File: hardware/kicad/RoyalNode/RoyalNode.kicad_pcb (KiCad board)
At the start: 4 copper layers, 85 x 75 mm, 14 parts, among them J1 XT30PW-M C431092 RC, J2 XT30PW-M C431092 RC, J5 SMA edge envelope, Q1 Infineon PG-DSO-8-27 thermal 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, Q2 Infineon PG-DSO-8-27 thermal 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, Q3 Infineon PG-DSO-8-27 thermal 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, U1 BQ25798 RQM0029A RC, U2 LM66100 DCK0006A SC70-6 RC, U3 TPS61088 RHL0020A thermal via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, U4 LTC4365 TSOT-23-8 RC

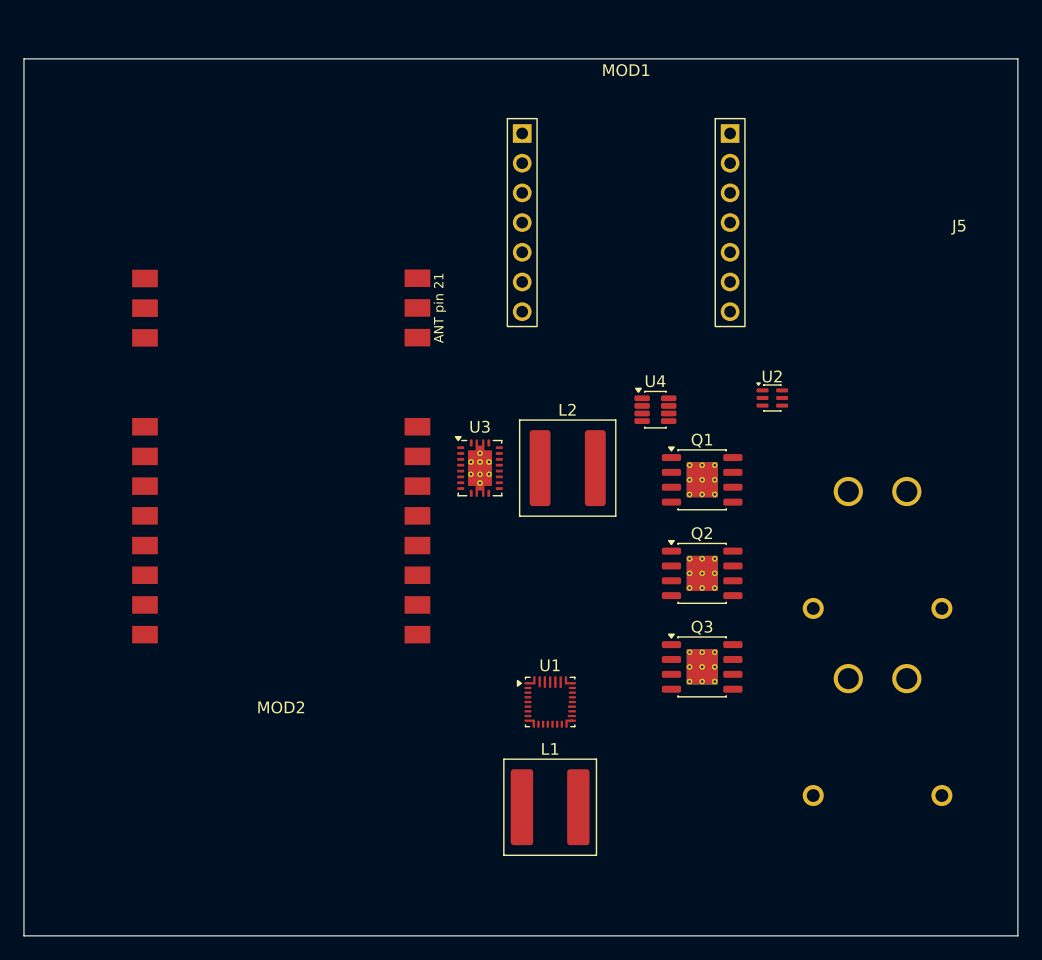
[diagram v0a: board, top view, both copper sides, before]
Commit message: Stage passive PCB footprints
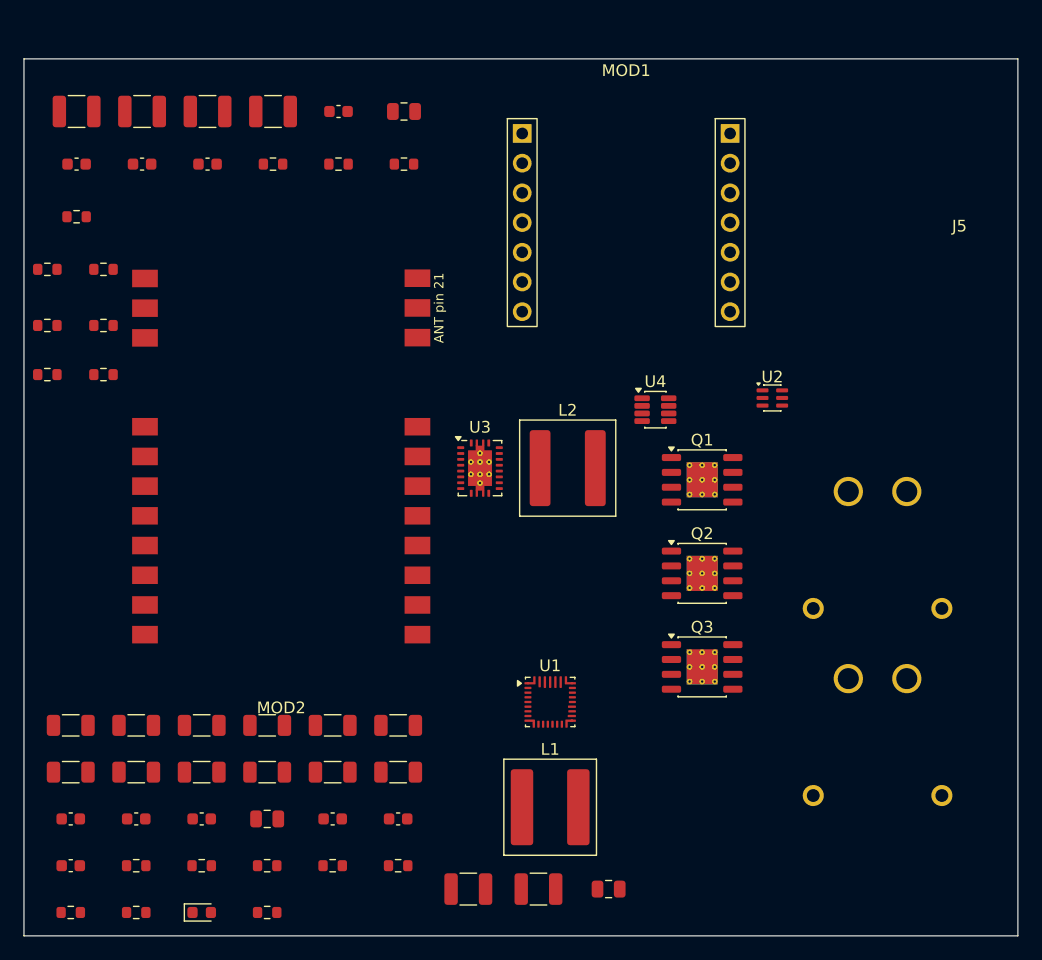
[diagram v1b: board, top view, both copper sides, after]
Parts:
- added C200: 10 uF 50 V, Capacitor_SMD:C_1206_3216Metric, F.Cu at (24.0, 77.0)
- added C201: 10 uF 50 V, Capacitor_SMD:C_1206_3216Metric, F.Cu at (29.6, 77.0)
- added C202: 10 uF 50 V, Capacitor_SMD:C_1206_3216Metric, F.Cu at (35.2, 77.0)
- added C203: 10 uF 50 V, Capacitor_SMD:C_1206_3216Metric, F.Cu at (40.8, 77.0)
- added C204: 10 uF 50 V, Capacitor_SMD:C_1206_3216Metric, F.Cu at (46.4, 77.0)
- added C205: 10 uF 50 V, Capacitor_SMD:C_1206_3216Metric, F.Cu at (52.0, 77.0)
- added C206: 10 uF 50 V, Capacitor_SMD:C_1206_3216Metric, F.Cu at (24.0, 81.0)
- added C207: 10 uF 50 V, Capacitor_SMD:C_1206_3216Metric, F.Cu at (29.6, 81.0)
- added C208: 10 uF 50 V, Capacitor_SMD:C_1206_3216Metric, F.Cu at (35.2, 81.0)
- added C209: 10 uF 50 V, Capacitor_SMD:C_1206_3216Metric, F.Cu at (40.8, 81.0)
- added C210: 10 uF 50 V, Capacitor_SMD:C_1206_3216Metric, F.Cu at (46.4, 81.0)
- added C211: 10 uF 50 V, Capacitor_SMD:C_1206_3216Metric, F.Cu at (52.0, 81.0)
- added C212: 100 nF 50 V, Capacitor_SMD:C_0603_1608Metric, F.Cu at (24.0, 85.0)
- added C213: 100 nF 50 V, Capacitor_SMD:C_0603_1608Metric, F.Cu at (29.6, 85.0)
- added C214: 100 nF 50 V, Capacitor_SMD:C_0603_1608Metric, F.Cu at (35.2, 85.0)
- added C215: 4.7 uF 25 V, Capacitor_SMD:C_0805_2012Metric, F.Cu at (40.8, 85.0)
- added C216: 47 nF 50 V, Capacitor_SMD:C_0603_1608Metric, F.Cu at (46.4, 85.0)
- added C217: 47 nF 50 V, Capacitor_SMD:C_0603_1608Metric, F.Cu at (52.0, 85.0)
- added C218: 1 nF 50 V, Capacitor_SMD:C_0603_1608Metric, F.Cu at (24.0, 89.0)
- added C400: 22 uF 16 V, Capacitor_SMD:C_1210_3225Metric, F.Cu at (24.5, 24.5)
- added C401: 22 uF 16 V, Capacitor_SMD:C_1210_3225Metric, F.Cu at (30.1, 24.5)
- added C402: 47 uF 10 V, Capacitor_SMD:C_1210_3225Metric, F.Cu at (35.7, 24.5)
- added C403: 47 uF 10 V, Capacitor_SMD:C_1210_3225Metric, F.Cu at (41.3, 24.5)
- added C404: 100 nF 50 V, Capacitor_SMD:C_0603_1608Metric, F.Cu at (46.9, 24.5)
- added C405: 2.2 uF, Capacitor_SMD:C_0805_2012Metric, F.Cu at (52.5, 24.5)
- added C406: 100 nF, Capacitor_SMD:C_0603_1608Metric, F.Cu at (24.5, 29.0)
- added C407: 47 nF, Capacitor_SMD:C_0603_1608Metric, F.Cu at (30.1, 29.0)
- added C408: 4.7 nF, Capacitor_SMD:C_0603_1608Metric, F.Cu at (35.7, 29.0)
- added C500: 22 uF 16 V, Capacitor_SMD:C_1210_3225Metric, F.Cu at (58.0, 91.0)
- added C501: 22 uF 16 V, Capacitor_SMD:C_1210_3225Metric, F.Cu at (64.0, 91.0)
- added C502: 1 uF 16 V, Capacitor_SMD:C_0805_2012Metric, F.Cu at (70.0, 91.0)
- added D1: Red 0603 LED, LED_SMD:LED_0603_1608Metric, F.Cu at (35.2, 93.0)
- added R100: 1.87 MOhm 1%, Resistor_SMD:R_0603_1608Metric, F.Cu at (22.0, 38.0)
- added R101: 104 kOhm 0.1%, Resistor_SMD:R_0603_1608Metric, F.Cu at (26.8, 38.0)
- added R102: 40.2 kOhm 0.1%, Resistor_SMD:R_0603_1608Metric, F.Cu at (22.0, 42.8)
- added R103: 100 kOhm, Resistor_SMD:R_0603_1608Metric, F.Cu at (26.8, 42.8)
- added R200: 5.23 kOhm 1%, Resistor_SMD:R_0603_1608Metric, F.Cu at (29.6, 89.0)
- added R201: 30.1 kOhm 1%, Resistor_SMD:R_0603_1608Metric, F.Cu at (35.2, 89.0)
- added R202: 100 Ohm, Resistor_SMD:R_0603_1608Metric, F.Cu at (40.8, 89.0)
- added R203: 4.70 kOhm 1%, Resistor_SMD:R_0603_1608Metric, F.Cu at (46.4, 89.0)
- added R204: 10 kOhm, Resistor_SMD:R_0603_1608Metric, F.Cu at (52.0, 89.0)
- added R205: 10 kOhm, Resistor_SMD:R_0603_1608Metric, F.Cu at (24.0, 93.0)
- added R206: 10 kOhm, Resistor_SMD:R_0603_1608Metric, F.Cu at (29.6, 93.0)
- added R207: 2.2 kOhm 1%, Resistor_SMD:R_0603_1608Metric, F.Cu at (40.8, 93.0)
- added R400: 176 kOhm 0.1%, Resistor_SMD:R_0603_1608Metric, F.Cu at (41.3, 29.0)
- added R401: 56.0 kOhm 0.1%, Resistor_SMD:R_0603_1608Metric, F.Cu at (46.9, 29.0)
- added R402: 330 kOhm, Resistor_SMD:R_0603_1608Metric, F.Cu at (52.5, 29.0)
- added R403: 100 kOhm, Resistor_SMD:R_0603_1608Metric, F.Cu at (24.5, 33.5)
- added R404: 20.0 kOhm, Resistor_SMD:R_0603_1608Metric, F.Cu at (26.8, 47.0)
- added R405: 100 kOhm, Resistor_SMD:R_0603_1608Metric, F.Cu at (22.0, 47.0)

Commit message: Standardize low-current connectors on JST-GH
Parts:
- added J3: J_LOW_JST_GH_SM02B_GHS_TB_RC, RoyalNode:J_LOW_JST_GH_SM02B_GHS_TB_RC, F.Cu at (92.0, 34.0)
- added J4: J_LOW_JST_GH_SM02B_GHS_TB_RC, RoyalNode:J_LOW_JST_GH_SM02B_GHS_TB_RC, F.Cu at (84.5, 88.5)

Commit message: Assign solar fuse footprint
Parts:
- added F1: F1_LITTELFUSE_483_1206_RC, RoyalNode:F1_LITTELFUSE_483_1206_RC, F.Cu at (87.0, 54.0)
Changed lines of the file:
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@@
+  	)
+  )
+  (footprint "RoyalNode:F1_LITTELFUSE_483_1206_RC"
+  	(version 20260206)
+  	(generator "kicad-footprint-generator")
+  	(layer "F.Cu")
+    (at 87.00 54.00 0)
+  	(descr "NOT_RELEASED_RELEASE_CANDIDATE Littelfuse 483 series 1206 chip fuse footprint copied from KiCad Fuse_1206_3216Metric; verify against Littelfuse 483 package drawing before release")
+  	(property "Reference" "F1"
+  		(at 0 -1.83 0)
+  		(layer "F.SilkS")
+  		(effects
+  			(font
+  				(size 1 1)
+  				(thickness 0.15)
+  			)
+  		)
+  	)
+  	(property "Value" "F1_LITTELFUSE_483_1206_RC"
+  		(at 0 1.83 0)
+  		(layer "F.Fab")
+  		(effects
+  			(font
+  				(size 1 1)
+  				(thickness 0.15)
+  			)
+  		)
+  	)
+  	(property "KiLib_Generator" "SMD_2terminal_chip_molded"
+  		(at 0 0 0)
+  		(layer "F.SilkS")
+  		(hide yes)
+  		(effects
+  			(font
+  				(size 1 1)
+  				(thickness 0.15)
+  			)
+  		)
+  	)
+  	(attr smd)
+  	(duplicate_pad_numbers_are_jumpers no)
+  	(fp_line
+  		(start -0.602064 -0.91)
+  		(end 0.602064 -0.91)
+  		(stroke
+  			(width 0.12)
+  			(type solid)
+  		)
+  		(layer "F.SilkS")
+  	)
+  	(fp_line
+  		(start -0.602064 0.91)
+  		(end 0.602064 0.91)
+  		(stroke
+  			(width 0.12)
+  			(type solid)
+  		)
+  		(layer "F.SilkS")
+  	)
+  	(fp_rect
+  		(start -2.28 -1.13)
+  		(end 2.28 1.13)
+  		(stroke
+  			(width 0.05)
+  			(type solid)
+  		)
+  		(fill no)
+  		(layer "F.CrtYd")
+  	)
+  	(fp_rect
+  		(start -1.6 -0.8)
+  		(end 1.6 0.8)
+  		(stroke
+  			(width 0.1)
+  			(type solid)
+  		)
+  		(fill no)
+  		(layer "F.Fab")
+  	)
+  	(fp_text user "${REFERENCE}"
+  		(at 0 0 0)
+  		(layer "F.Fab")
+  		(effects
+  			(font
+  				(size 0.8 0.8)
+  				(thickness 0.12)
+  			)
+  		)
+  	)
+  	(pad "1" smd roundrect
+  		(at -1.4 0)
+  		(size 1.25 1.75)
+  		(layers "F.Cu" "F.Mask" "F.Paste")
+  		(roundrect_rratio 0.2)
+		(net 7 "SOLAR_RAW")
+		(pinfunction "Terminal 1"))
+  	(pad "2" smd roundrect
+  		(at 1.4 0)
+  		(size 1.25 1.75)
+  		(layers "F.Cu" "F.Mask" "F.Paste")
+  		(roundrect_rratio 0.2)
+		(net 8 "SOLAR_FUSED")
+		(pinfunction "Terminal 2"))
+  	(embedded_fonts no)
+  	(model "${KICAD10_3DMODEL_DIR}/Fuse.3dshapes/Fuse_1206_3216Metric.step"
+  		(offset
+  			(xyz 0 0 0)
+  		)
+  		(scale
+  			(xyz 1 1 1)
+  		)
+  		(rotate
+  			(xyz 0 0 0)
+  		)
   	)
   )

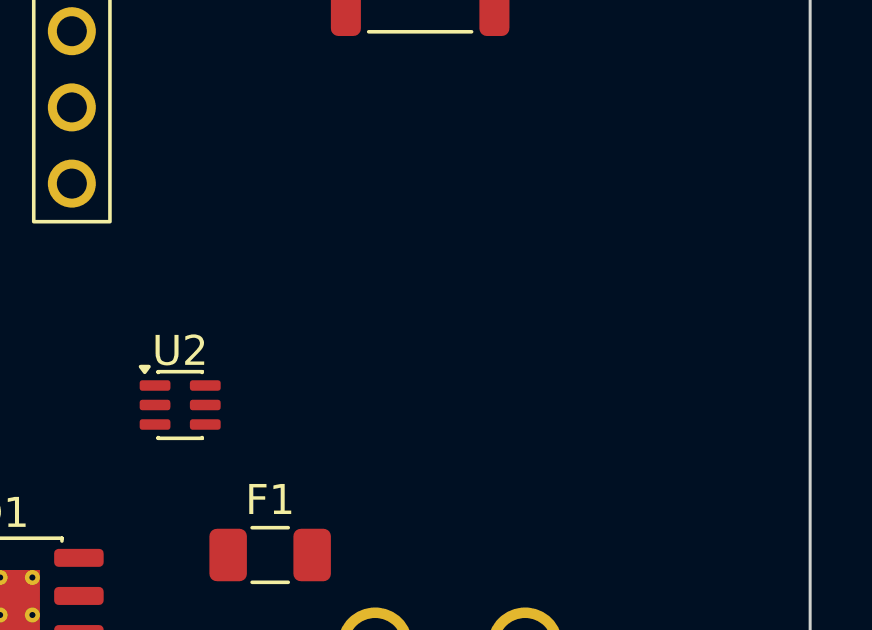
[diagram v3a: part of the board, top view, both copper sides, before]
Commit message: Assign E22 bulk capacitor footprint
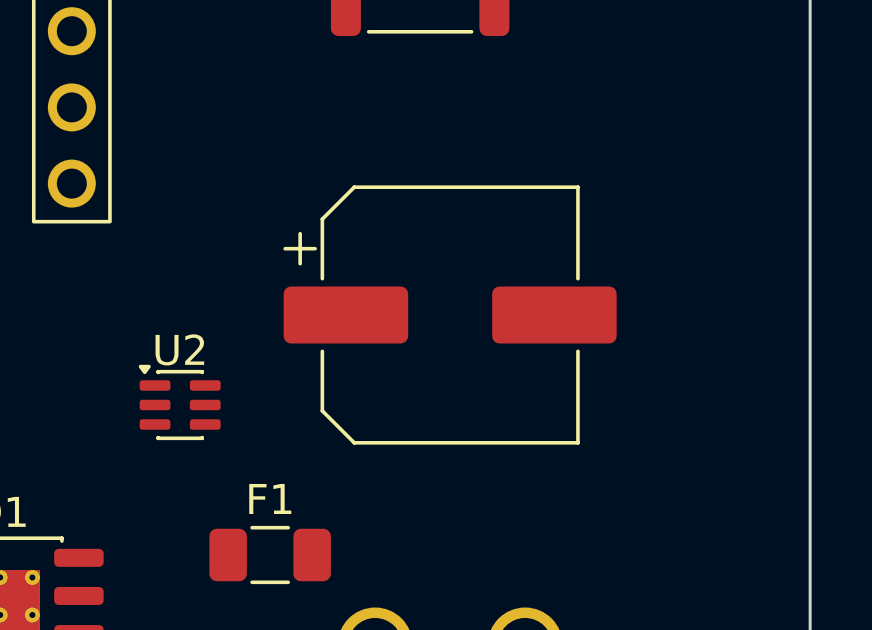
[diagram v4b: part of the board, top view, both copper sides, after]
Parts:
- added C503: 330 uF 10 V polymer, RoyalNode:C503_PANASONIC_10SVPC330M_8X6P9_RC, F.Cu at (93.0, 46.0)

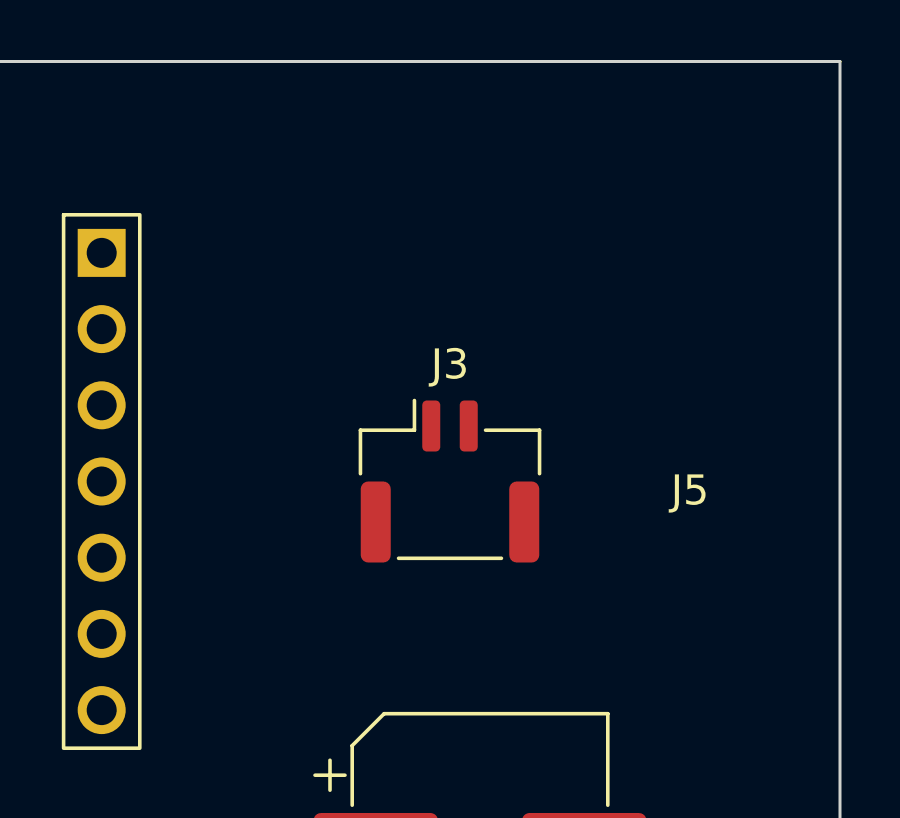
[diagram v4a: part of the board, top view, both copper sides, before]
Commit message: Add optional BME680 I2C connector
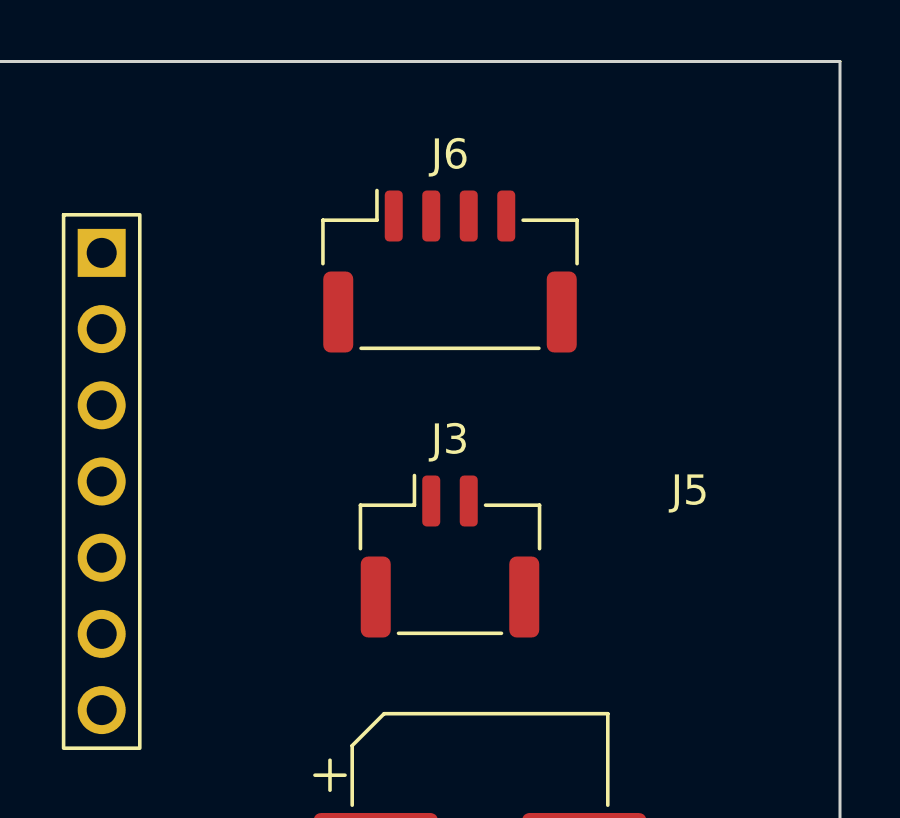
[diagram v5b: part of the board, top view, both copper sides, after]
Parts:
- added J6: J_LOW_JST_GH_SM04B_GHS_TB_RC, RoyalNode:J_LOW_JST_GH_SM04B_GHS_TB_RC, F.Cu at (92.0, 27.0)
- moved J3 2.50 mm to (92.0, 36.5)

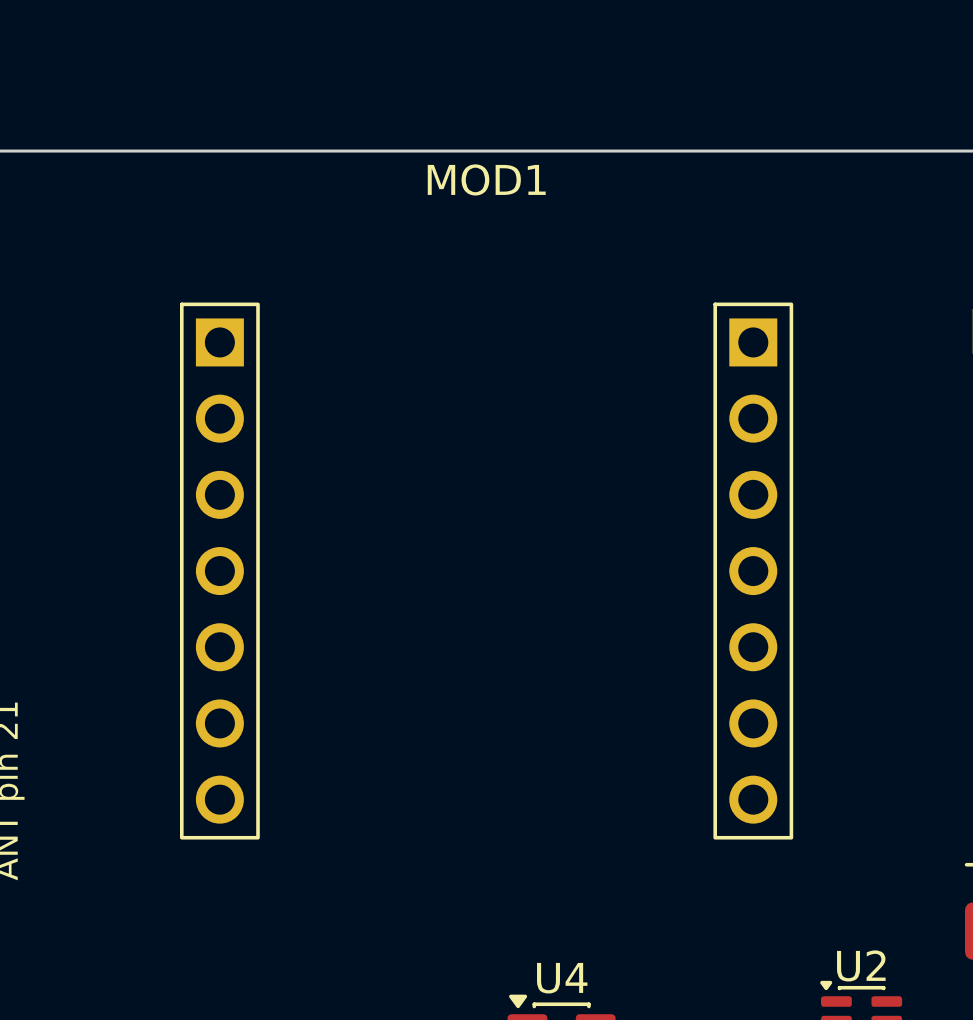
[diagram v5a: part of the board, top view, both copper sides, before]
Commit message: Shift XIAO socket above RF corridor
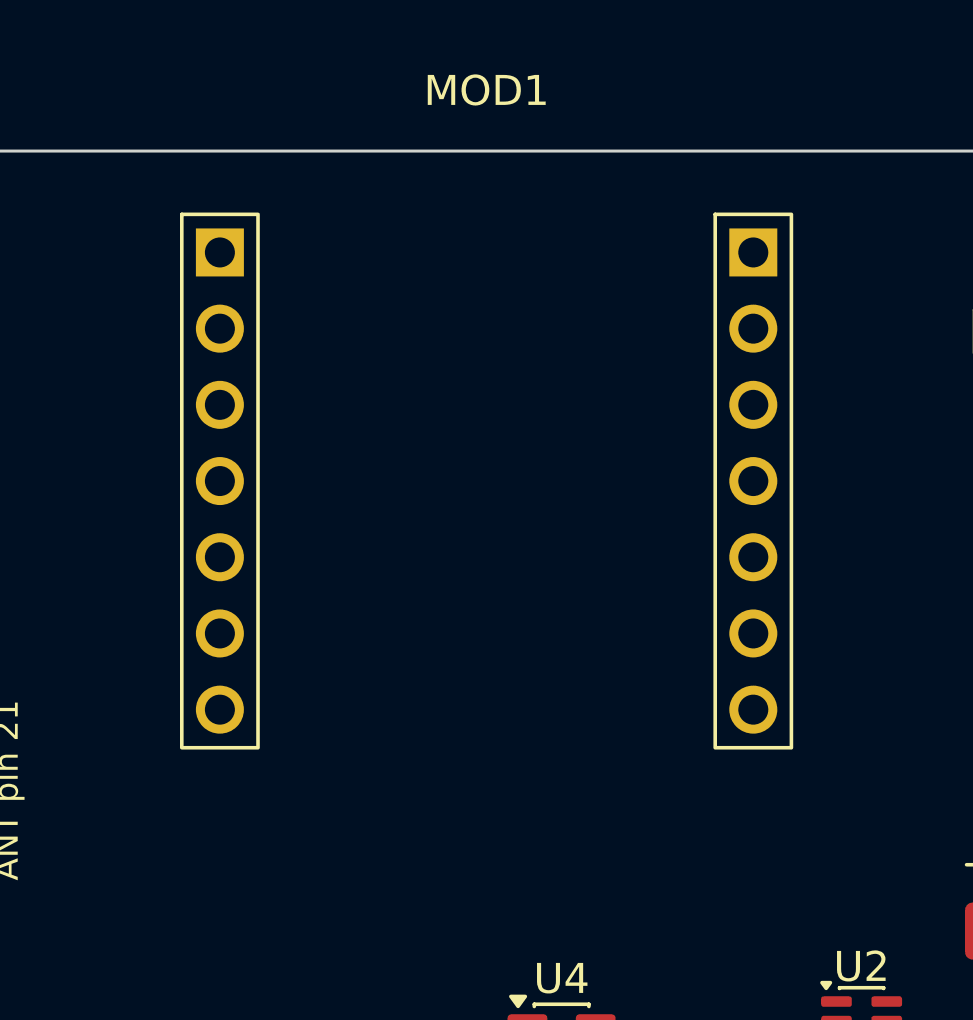
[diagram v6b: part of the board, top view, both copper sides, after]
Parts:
- moved MOD1 3.00 mm to (71.5, 31.0)
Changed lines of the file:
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@@
     (generator "royalnode")
     (generator_version "1")
-    (at 71.50 34.00 0)
+    (at 71.50 31.00 0)
     (layer "F.Cu")
     (descr "NOT_RELEASED_RELEASE_CANDIDATE composite socket footprint for Seeed XIAO nRF52840 using two LXWCONN 254PM-1x7P-V C53202181 socket strips")
